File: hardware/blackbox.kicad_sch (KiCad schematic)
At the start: 5 parts

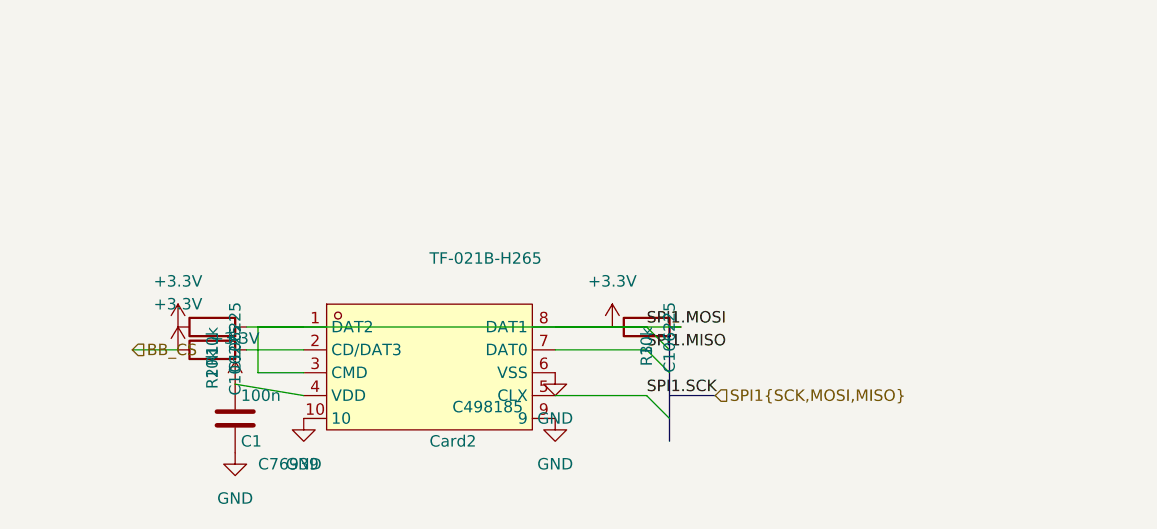
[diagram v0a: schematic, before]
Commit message: WIP: schematic updates, library modernization, audit tooling
Schematic changes (user):
- Add ADC bypass caps on CURRENT/RSSI/EXTERNAL (1k + 100nF RC filter)
- Add IMU GYRO_CS 10k pull-up to +3.3V
- Reverse P1 ESC 8-pin JST SH pinout to BF standard
  (pin1=V+, pin2=GND, pin3=Current, pin5-8=M1-M4)
- SD card (blackbox) sub-sheet with SPI1 + FLASH_CS + decoupling
- Other sub-sheet cleanup (rp2350a, osd, pads, power, imu)

Footprint library:
- Convert all 62 legacy (module ...) footprints to modern
  (footprint ...) format via pcbnew API — fixes kicad-sch-api
  "footprint not found" errors

Tooling:
- Add hardware/tools/audit_design.py (BF-rule design audit script)
- Add hardware/tools/design_audit.md (audit report output)

Docs:
- Update CLAUDE.md: current GPIO map, corrected power tree net names,
  open issues list (CRIT-2..5), connector verification status

Co-Authored-By: Claude Opus 4.6 (1M context) <noreply@anthropic.com>
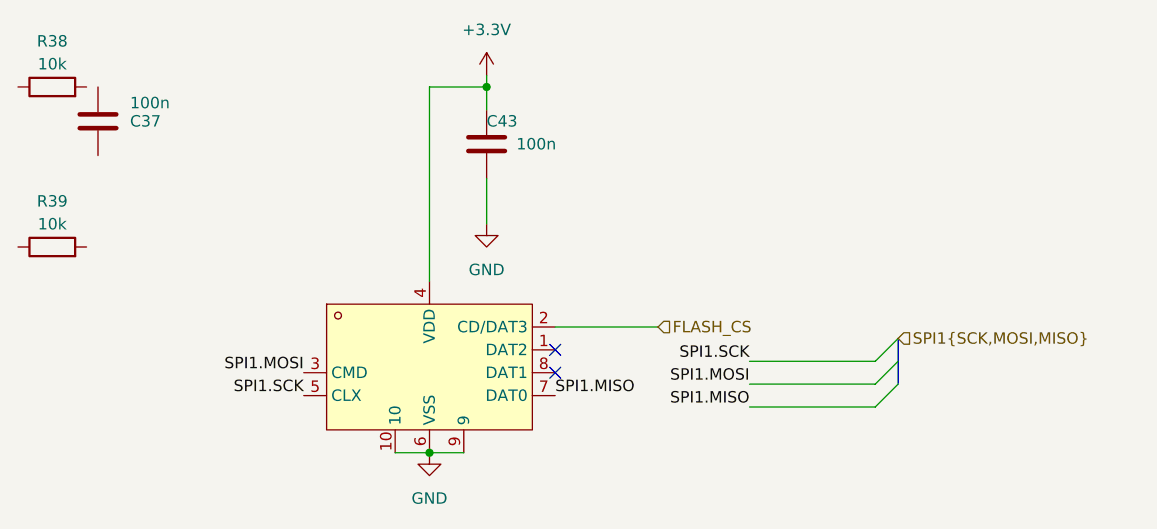
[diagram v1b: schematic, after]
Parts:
- removed C1: 100n, Capacitor_SMD:C_0201_0603Metric, symbol Device:C
- removed R1, R2, R3: 10k, Capacitor_SMD:C_0201_0603Metric, symbol Device:R
- added C37, C43: 100n, Capacitor_SMD:C_0201_0603Metric, symbol Device:C
- added R38, R39: 10k, Capacitor_SMD:C_0201_0603Metric, symbol Device:R
- renumbered Card2 to Card1
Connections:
- net +3.3V: now also C43.1
- net GND: now also C43.2
- net SPI1.MOSI: no longer Card1.1 (DAT2), Card1.8 (DAT1)
- net FLASH_CS: now reaches Card1.2 (CD/DAT3)
- no-connect marks 0 -> 2

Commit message: V0.3 routed: pin remap, footprint fixes, EMC checklist, DFM prep
Schematic (user):
- OSD pins remapped to GPIO4-6 (OSD_W/OSD_EN/OSD_SYNC consecutive
  for FB_OSD PIO driver per BF PR#14882)
- SBUS inverter stays on GPIO9 (valid UART1_RX)
- Beeper moved to GPIO36
- Various sub-sheet updates

PCB:
- Full board routed, bottom-side component placement
- Resistor footprints: C_0201 -> R_0201 for correct 3D models
- Capacitor 3D model paths fixed (were pointing to R_0201)
- SD card footprint 3D path fixed (${KIPRJMOD}/lib.3dshapes/)
- 2 footprint 3D paths fixed (SIM, TF-01A: /lib.3dshapes -> ${KIPRJMOD})

Tooling & docs:
- Add EMC checklist (hardware/tools/EMC_CHECKLIST.md)
- Add EMC note script (hardware/tools/add_emc_note.py)
- Update CLAUDE.md: LMR51430 drop-in upgrade noted, connector
  verification, OSD pin mapping

Co-Authored-By: Claude Opus 4.6 (1M context) <noreply@anthropic.com>
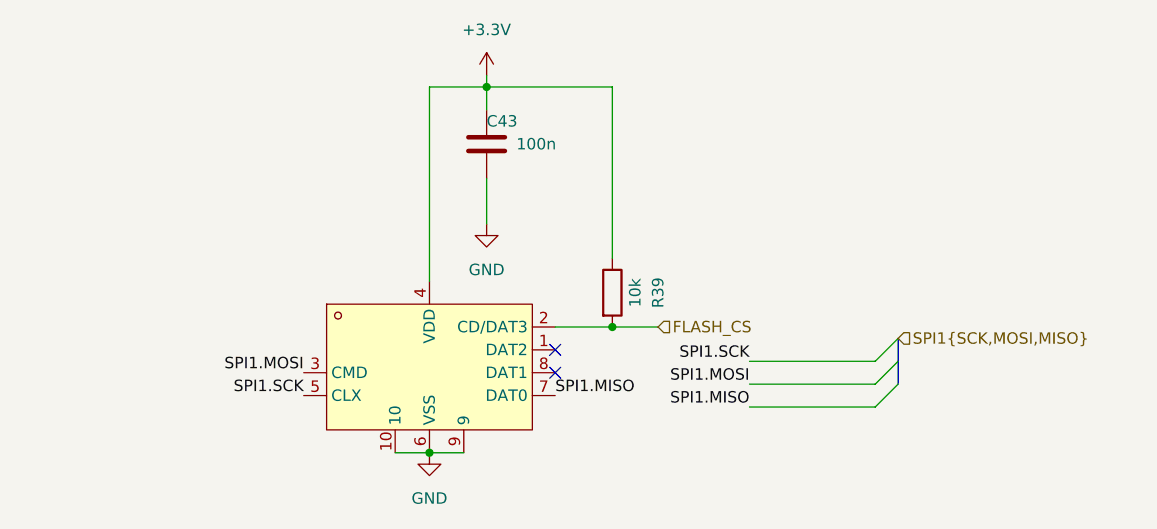
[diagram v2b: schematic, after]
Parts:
- removed C37: 100n, Capacitor_SMD:C_0201_0603Metric, symbol Device:C
- removed R38: 10k, Capacitor_SMD:C_0201_0603Metric, symbol Device:R
- R39: footprint Capacitor_SMD:C_0201_0603Metric -> Resistor_SMD:R_0201_0603Metric
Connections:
- net +3.3V: now also R39.1
- net FLASH_CS: now also R39.2
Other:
- moved on the sheet: R39

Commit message: Add V0.3 known issues for V0.4 fix list, update open issues
C28 voltage rating, R30 divider, L2 inductor value, LED0 color,
LMR51430 upgrade path — all noted for next revision. CRIT-5 (ESC
connector) marked fixed. OSD pin mapping updated to GPIO4-6.

Co-Authored-By: Claude Opus 4.6 (1M context) <noreply@anthropic.com>
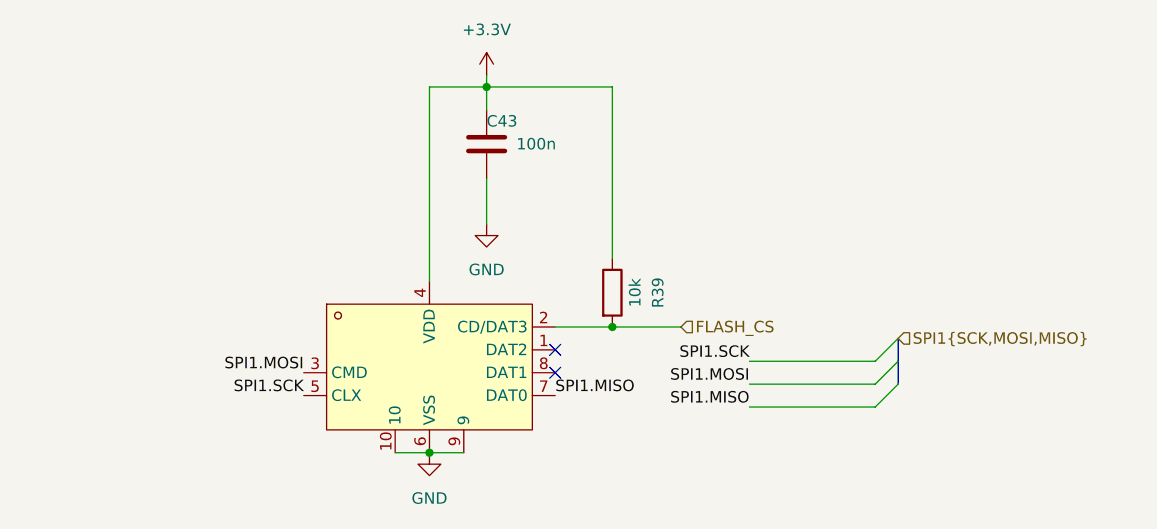
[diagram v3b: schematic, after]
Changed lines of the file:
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@@
 	(wire
 		(pts
-			(xy 135.89 71.12) (xy 140.97 71.12)
+			(xy 135.89 71.12) (xy 143.51 71.12)
 		)
 		(stroke
@@
 	(hierarchical_label "FLASH_CS"
 		(shape input)
-		(at 140.97 71.12 0)
+		(at 143.51 71.12 0)
 		(effects
 			(font
